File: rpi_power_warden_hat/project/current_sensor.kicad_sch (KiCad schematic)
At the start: 5 parts, among them U1 INA260

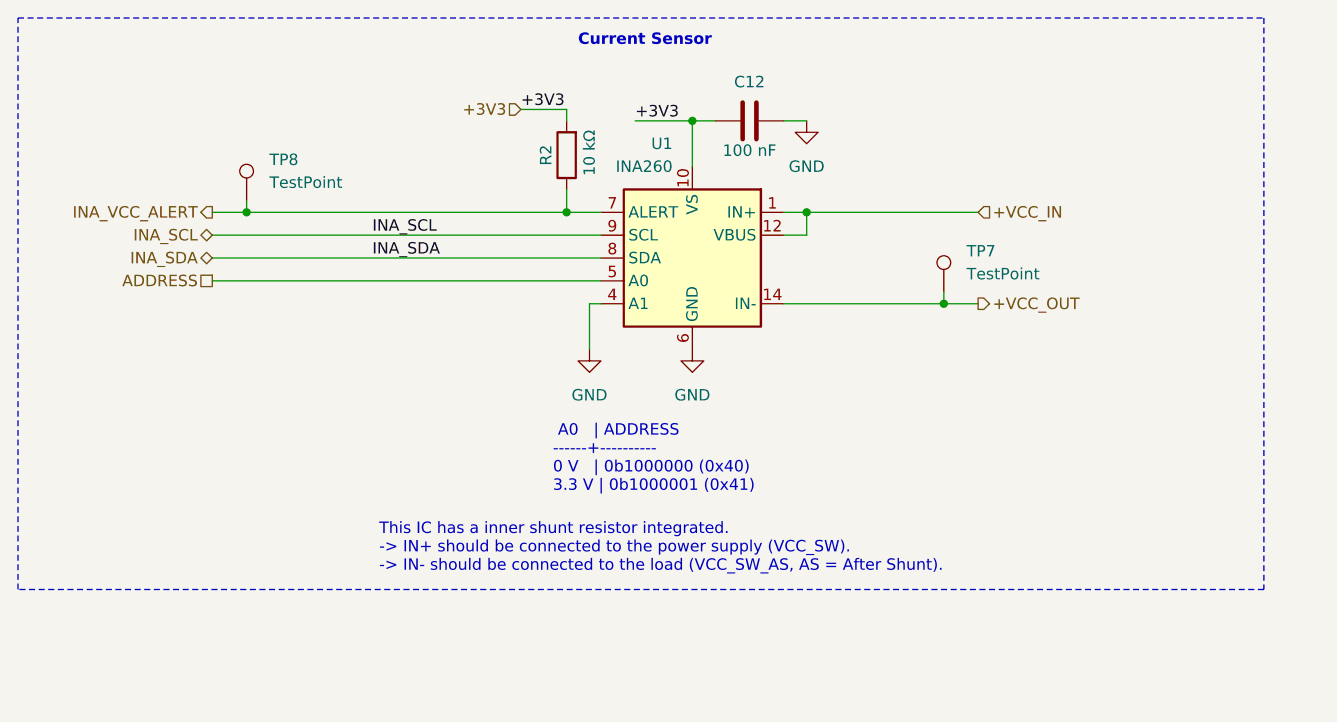
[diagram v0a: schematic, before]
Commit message: re-annotate schematic, add leds to power supply outputs and add connector for VBAT switched load
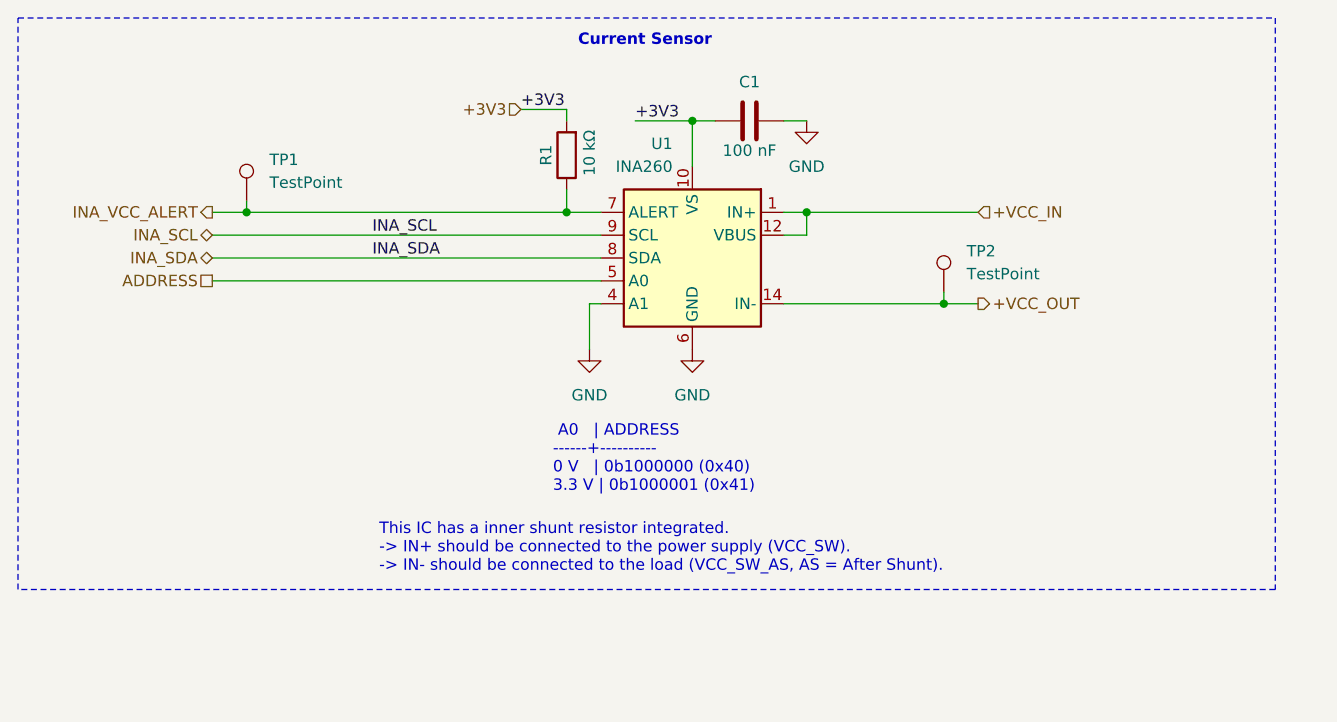
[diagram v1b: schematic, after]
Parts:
- renumbered C12 to C1, R2 to R1, TP8 to TP1, TP7 to TP2
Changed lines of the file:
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@@
 	(rectangle
 		(start 63.5 50.8)
-		(end 201.93 114.3)
+		(end 203.2 114.3)
 		(stroke
 			(width 0)
@@
 		(on_board yes)
 		(dnp no)
-		(property "Reference" "R2"
+		(property "Reference" "R1"
 			(at 122.174 66.04 90)
 			(effects
@@
 		(dnp no)
 		(fields_autoplaced yes)
-		(property "Reference" "#PWR11"
+		(property "Reference" "#PWR7"
 			(at 151.13 68.58 0)
 			(effects
@@
 			(project "rpi_power_warden_hat"
 				(path "/8692c5de-a943-41e8-8e29-f6c5e99cda34/280f8587-5166-4f13-bc2f-0b642f6ac80b"
-					(reference "#PWR17")
+					(reference "#PWR7")
 					(unit 1)
 				)
 				(path "/8692c5de-a943-41e8-8e29-f6c5e99cda34/52241f92-cbdb-484e-bc49-950aa69fc821"
-					(reference "#PWR11")
+					(reference "#PWR10")
 					(unit 1)
 				)
@@
 		(dnp no)
 		(fields_autoplaced yes)
-		(property "Reference" "TP8"
+		(property "Reference" "TP1"
 			(at 91.44 66.5479 0)
 			(effects
@@
 			(project "rpi_power_warden_hat"
 				(path "/8692c5de-a943-41e8-8e29-f6c5e99cda34/280f8587-5166-4f13-bc2f-0b642f6ac80b"
-					(reference "TP9")
+					(reference "TP1")
 					(unit 1)
 				)
 				(path "/8692c5de-a943-41e8-8e29-f6c5e99cda34/52241f92-cbdb-484e-bc49-950aa69fc821"
-					(reference "TP8")
+					(reference "TP3")
 					(unit 1)
 				)
@@
 		(dnp no)
 		(fields_autoplaced yes)
-		(property "Reference" "TP7"
+		(property "Reference" "TP2"
 			(at 168.91 76.7079 0)
 			(effects
@@
 			(project "rpi_power_warden_hat"
 				(path "/8692c5de-a943-41e8-8e29-f6c5e99cda34/280f8587-5166-4f13-bc2f-0b642f6ac80b"
-					(reference "TP10")
+					(reference "TP2")
 					(unit 1)
 				)
 				(path "/8692c5de-a943-41e8-8e29-f6c5e99cda34/52241f92-cbdb-484e-bc49-950aa69fc821"
-					(reference "TP7")
+					(reference "TP4")
 					(unit 1)
 				)
@@
 		(dnp no)
 		(fields_autoplaced yes)
-		(property "Reference" "#PWR8"
+		(property "Reference" "#PWR6"
 			(at 138.43 93.98 0)
 			(effects
@@
 			(project "rpi_power_warden_hat"
 				(path "/8692c5de-a943-41e8-8e29-f6c5e99cda34/280f8587-5166-4f13-bc2f-0b642f6ac80b"
-					(reference "#PWR12")
+					(reference "#PWR6")
 					(unit 1)
 				)
 				(path "/8692c5de-a943-41e8-8e29-f6c5e99cda34/52241f92-cbdb-484e-bc49-950aa69fc821"
-					(reference "#PWR8")
+					(reference "#PWR9")
 					(unit 1)
 				)
@@
 		(on_board yes)
 		(dnp no)
-		(property "Reference" "C12"
+		(property "Reference" "C1"
 			(at 144.78 57.912 90)
 			(effects
@@
 				)
 				(path "/8692c5de-a943-41e8-8e29-f6c5e99cda34/52241f92-cbdb-484e-bc49-950aa69fc821"
-					(reference "C12")
+					(reference "C2")
 					(unit 1)
 				)
@@
 			(project "rpi_power_warden_hat"
 				(path "/8692c5de-a943-41e8-8e29-f6c5e99cda34/280f8587-5166-4f13-bc2f-0b642f6ac80b"
-					(reference "U3")
+					(reference "U1")
 					(unit 1)
 				)
 				(path "/8692c5de-a943-41e8-8e29-f6c5e99cda34/52241f92-cbdb-484e-bc49-950aa69fc821"
-					(reference "U1")
+					(reference "U2")
 					(unit 1)
 				)
@@
 		(dnp no)
 		(fields_autoplaced yes)
-		(property "Reference" "#PWR4"
+		(property "Reference" "#PWR5"
 			(at 127 93.98 0)
 			(effects
@@
 			(project "rpi_power_warden_hat"
 				(path "/8692c5de-a943-41e8-8e29-f6c5e99cda34/280f8587-5166-4f13-bc2f-0b642f6ac80b"
-					(reference "#PWR10")
+					(reference "#PWR5")
 					(unit 1)
 				)
 				(path "/8692c5de-a943-41e8-8e29-f6c5e99cda34/52241f92-cbdb-484e-bc49-950aa69fc821"
-					(reference "#PWR4")
-					(unit 1)
-				)
+					(reference "#PWR8")
+					(unit 1)
+				)

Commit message: re-annotate schematic
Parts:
- renumbered TP1 to TP2, TP2 to TP3
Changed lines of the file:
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@@
 		(dnp no)
 		(fields_autoplaced yes)
-		(property "Reference" "TP1"
+		(property "Reference" "TP2"
 			(at 91.44 66.5479 0)
 			(effects
@@
 			(project "rpi_power_warden_hat"
 				(path "/8692c5de-a943-41e8-8e29-f6c5e99cda34/280f8587-5166-4f13-bc2f-0b642f6ac80b"
-					(reference "TP1")
+					(reference "TP2")
 					(unit 1)
 				)
 				(path "/8692c5de-a943-41e8-8e29-f6c5e99cda34/52241f92-cbdb-484e-bc49-950aa69fc821"
-					(reference "TP3")
+					(reference "TP4")
 					(unit 1)
 				)
@@
 		(dnp no)
 		(fields_autoplaced yes)
-		(property "Reference" "TP2"
+		(property "Reference" "TP3"
 			(at 168.91 76.7079 0)
 			(effects
@@
 			(project "rpi_power_warden_hat"
 				(path "/8692c5de-a943-41e8-8e29-f6c5e99cda34/280f8587-5166-4f13-bc2f-0b642f6ac80b"
-					(reference "TP2")
+					(reference "TP3")
 					(unit 1)
 				)
 				(path "/8692c5de-a943-41e8-8e29-f6c5e99cda34/52241f92-cbdb-484e-bc49-950aa69fc821"
-					(reference "TP4")
+					(reference "TP5")
 					(unit 1)
 				)

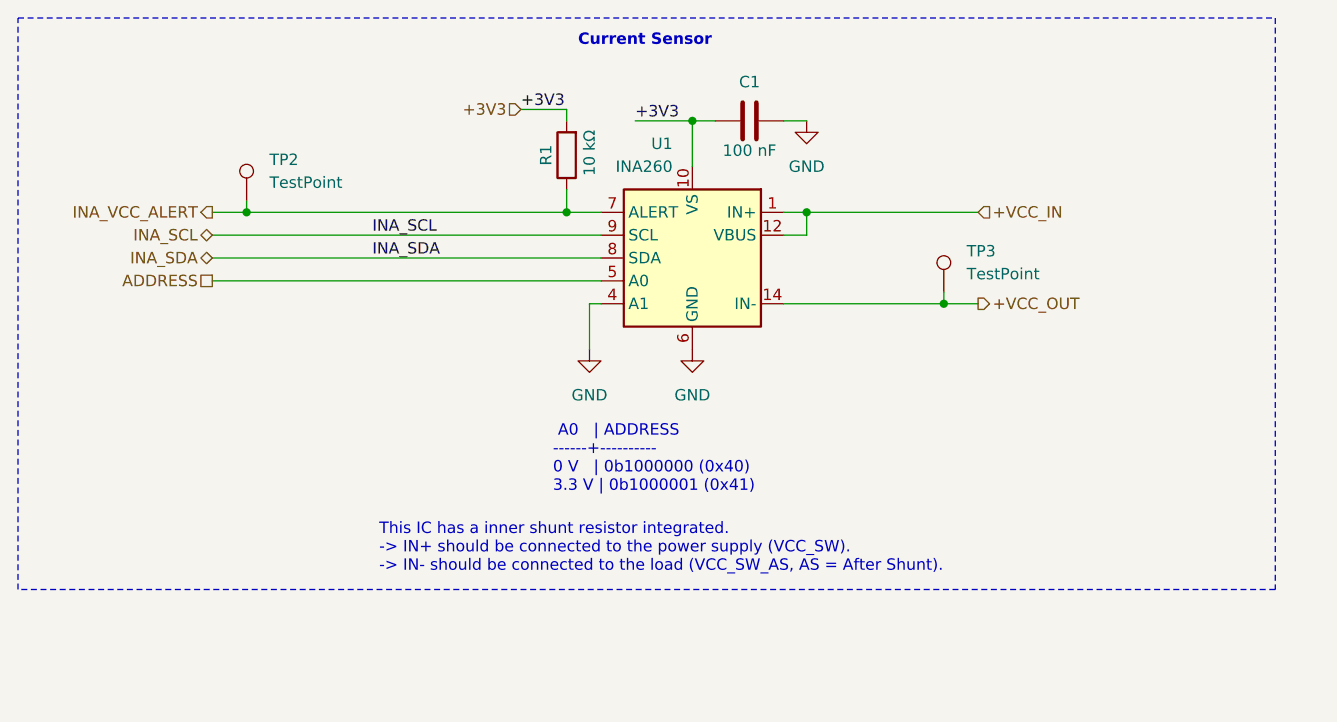
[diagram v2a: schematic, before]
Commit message: add and gate in swiched power supplies enable
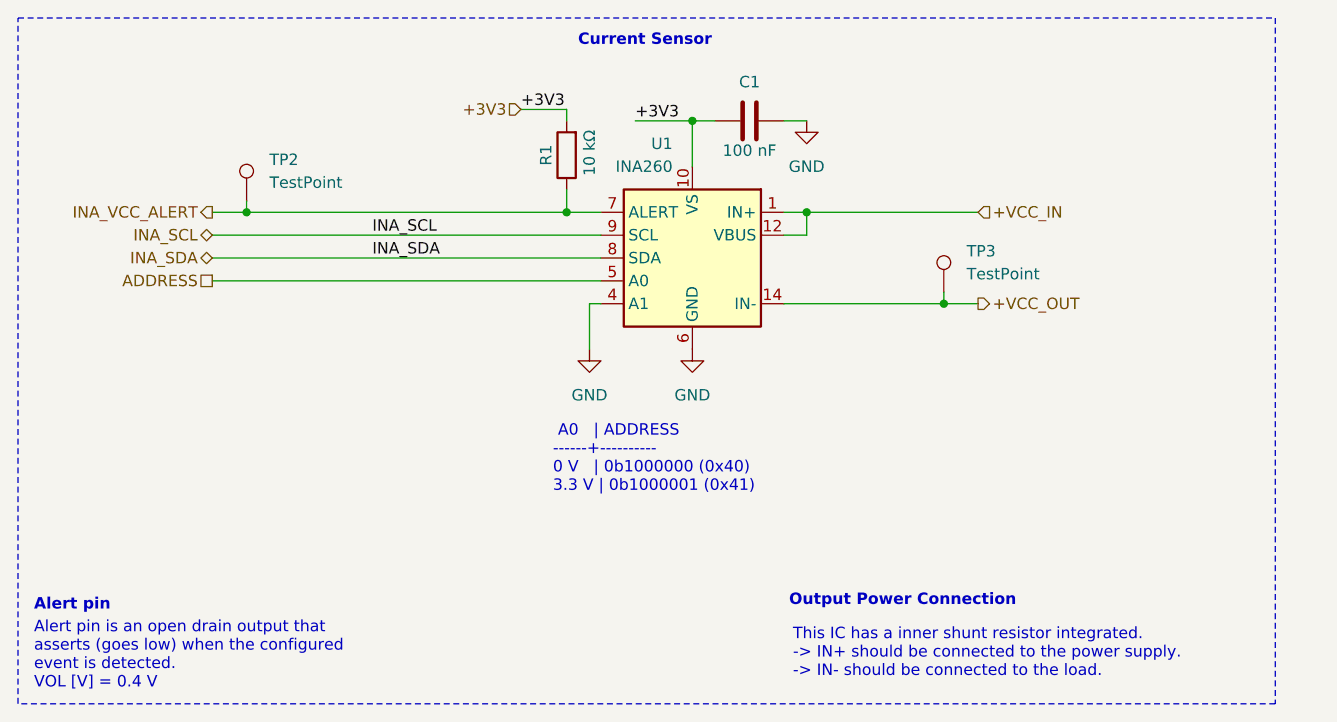
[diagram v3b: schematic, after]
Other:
- note added: "Alert pin"
- note added: "Alert pin is an open drain output that asserts (goes low) when the configured event is detected. VOL [V] = 0.4 V"
- note added: "Output Power Connection"
- note added: "This IC has a inner shunt resistor integrated. -> IN+ should be connected to the power supply. -> IN- should be connected to the load."
- note removed: "This IC has a inner shunt resistor integrated. -> IN+ should be connected to the power supply (VCC_SW). -> IN- should be connected to the load (VCC_SW_AS, AS = After Shunt)."
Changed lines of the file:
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@@
 	(rectangle
 		(start 63.5 50.8)
-		(end 203.2 114.3)
+		(end 203.2 127)
 		(stroke
 			(width 0)
@@
 		)
 	)
-	(text "This IC has a inner shunt resistor integrated.\n-> IN+ should be connected to the power supply (VCC_SW).\n-> IN- should be connected to the load (VCC_SW_AS, AS = After Shunt)."
+	(text "Alert pin is an open drain output that \nasserts (goes low) when the configured \nevent is detected.\nVOL [V] = 0.4 V"
 		(exclude_from_sim no)
-		(at 103.632 109.728 0)
+		(at 65.278 121.666 0)
+		(effects
+			(font
+				(size 1.27 1.27)
+			)
+			(justify left)
+		)
+	)
+	(text "Alert pin\n"
+		(exclude_from_sim no)
+		(at 65.278 116.078 0)
+		(effects
+			(font
+				(size 1.27 1.27)
+				(thickness 0.254)
+				(bold yes)
+			)
+			(justify left)
+		)
+	)
+	(text "This IC has a inner shunt resistor integrated.\n-> IN+ should be connected to the power supply.\n-> IN- should be connected to the load.\n"
+		(exclude_from_sim no)
+		(at 149.606 121.412 0)
 		(effects
 			(font
@@
 		)
 	)
+	(text "Output Power Connection"
+		(exclude_from_sim no)
+		(at 161.798 115.57 0)
+		(effects
+			(font
+				(size 1.27 1.27)
+				(thickness 0.254)
+				(bold yes)
+			)
+		)
+	)
